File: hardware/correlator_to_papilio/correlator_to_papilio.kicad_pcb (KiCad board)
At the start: 4 copper layers, 67.6 x 53.3 mm, 2 parts, among them J1 Papilio Pro, U1 TART Correlator SODIMM

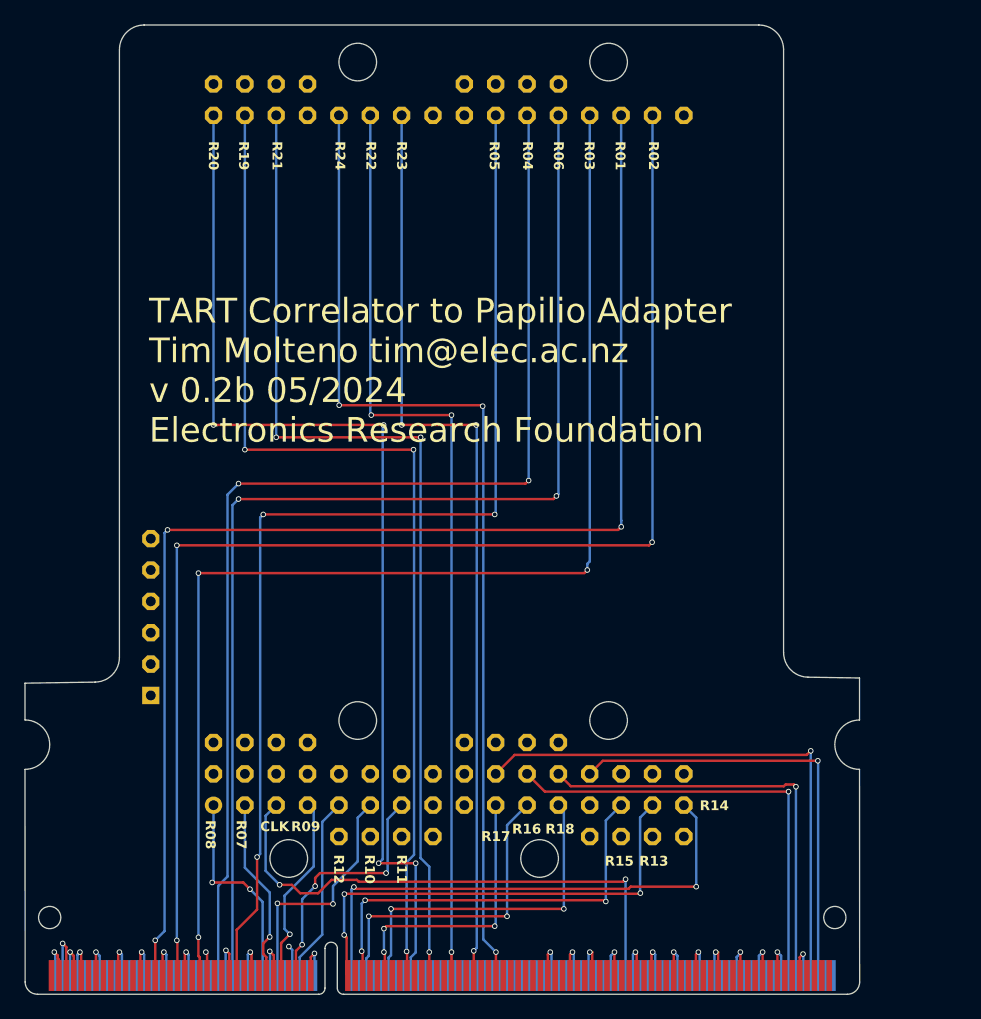
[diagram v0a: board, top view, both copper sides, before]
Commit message: Update the footprints and layout
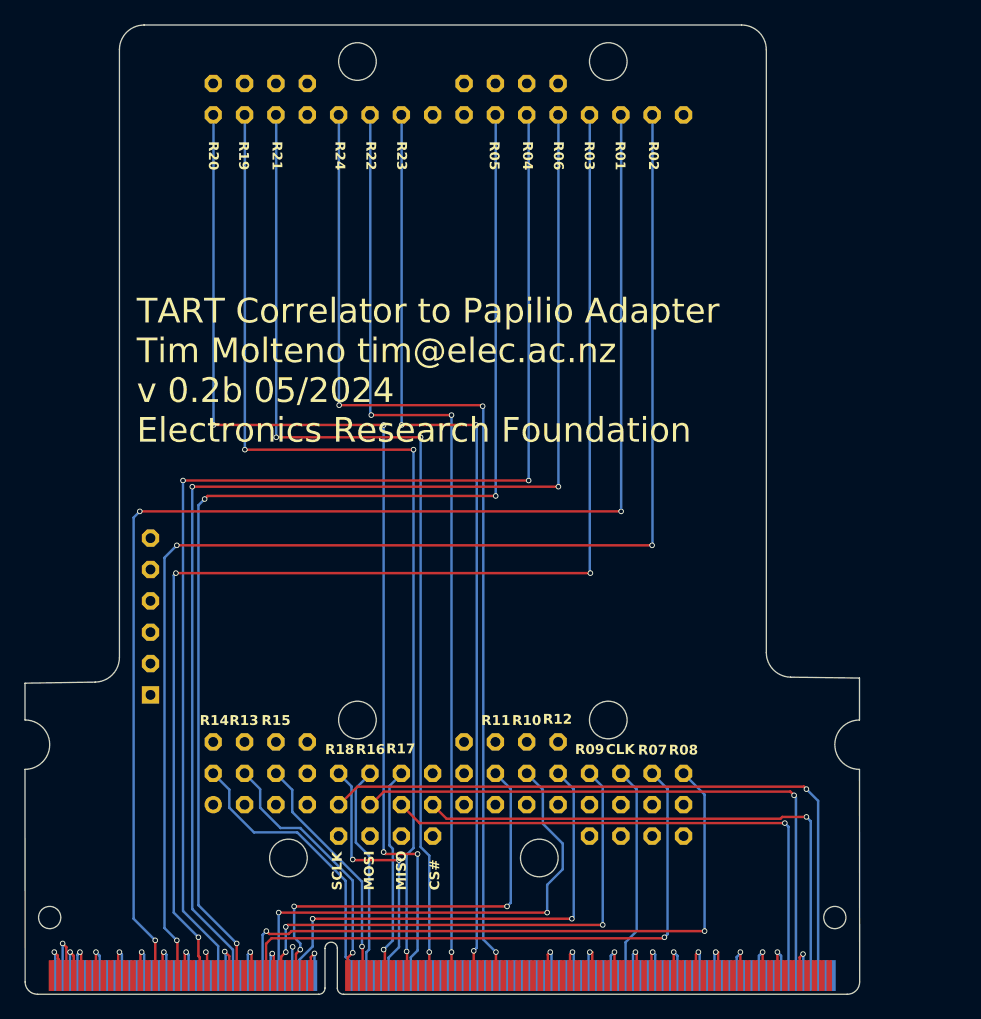
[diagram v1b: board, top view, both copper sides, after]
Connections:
- J1 pad A0: R14_I1 -> unconnected-(J1-PadA0)
- J1 pad A1: R13_I1 -> unconnected-(J1-PadA1)
- J1 pad A10: R10_I1 -> FPGA_MOSI
- J1 pad A11: R12_I1 -> FPGA_SCLK
- J1 pad A12: R09_I1 -> unconnected-(J1-PadA12)
- J1 pad A13: CLK_16 -> unconnected-(J1-PadA13)
- J1 pad A14: R07_I1 -> unconnected-(J1-PadA14)
- J1 pad A15: R08_I1 -> unconnected-(J1-PadA15)
- J1 pad A2: R15_I1 -> unconnected-(J1-PadA2)
- J1 pad A4: R18_I1 -> unconnected-(J1-PadA4)
- J1 pad A5: R16_I1 -> unconnected-(J1-PadA5)
- J1 pad A6: R17_I1 -> unconnected-(J1-PadA6)
- J1 pad A8: unconnected-(J1-PadA8) -> FPGA_CS#
- J1 pad A9: R11_I1 -> FPGA_MISO
- J1 pad B0: unconnected-(J1-PadB0) -> R14_I1
- J1 pad B1: unconnected-(J1-PadB1) -> R13_I1
- J1 pad B10: FPGA_MISO -> R10_I1
- J1 pad B11: FPGA_MOSI -> R12_I1
- J1 pad B12: FPGA_SCLK -> R09_I1
- J1 pad B13: unconnected-(J1-PadB13) -> CLK_16
- J1 pad B14: unconnected-(J1-PadB14) -> R07_I1
- J1 pad B15: unconnected-(J1-PadB15) -> R08_I1
- J1 pad B2: unconnected-(J1-PadB2) -> R15_I1
- J1 pad B4: unconnected-(J1-PadB4) -> R18_I1
- J1 pad B5: unconnected-(J1-PadB5) -> R16_I1
- J1 pad B6: unconnected-(J1-PadB6) -> R17_I1
- J1 pad B9: FPGA_CS# -> R11_I1
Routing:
- net R08_I1: track 17.0 -> 52.9 mm
- net R07_I1: track 15.0 -> 48.9 mm
- net R09_I1: track 15.5 -> 42.5 mm, vias 1 -> 3
- net CLK_16: track 44.0 -> 17.2 mm, vias 2 -> 0
- net R12_I1: track 15.1 -> 38.4 mm, vias 0 -> 2
- net R10_I1: track 19.6 -> 39.9 mm
- net R14_I1: track 42.1 -> 23.0 mm, vias 2 -> 0
- net FPGA_SCLK: track 36.3 -> 54.1 mm
- net R13_I1: track 38.3 -> 21.1 mm, vias 3 -> 1
- net R15_I1: track 34.1 -> 19.2 mm, vias 3 -> 1
- net FPGA_MOSI: track 35.1 -> 49.6 mm
- net R11_I1: track 20.5 -> 34.6 mm
- net R16_I1: track 25.8 -> 17.4 mm, vias 2 -> 0
- net FPGA_MISO: track 36.7 -> 44.1 mm
- net R18_I1: track 28.1 -> 20.9 mm
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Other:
- outline, holes or cut-outs redrawn
- board text added: "CS#"
- board text added: "MISO"
- board text added: "MOSI"
- board text added: "SCLK"

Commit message: Fix radio 4, and radio 7 being on the wrong pins
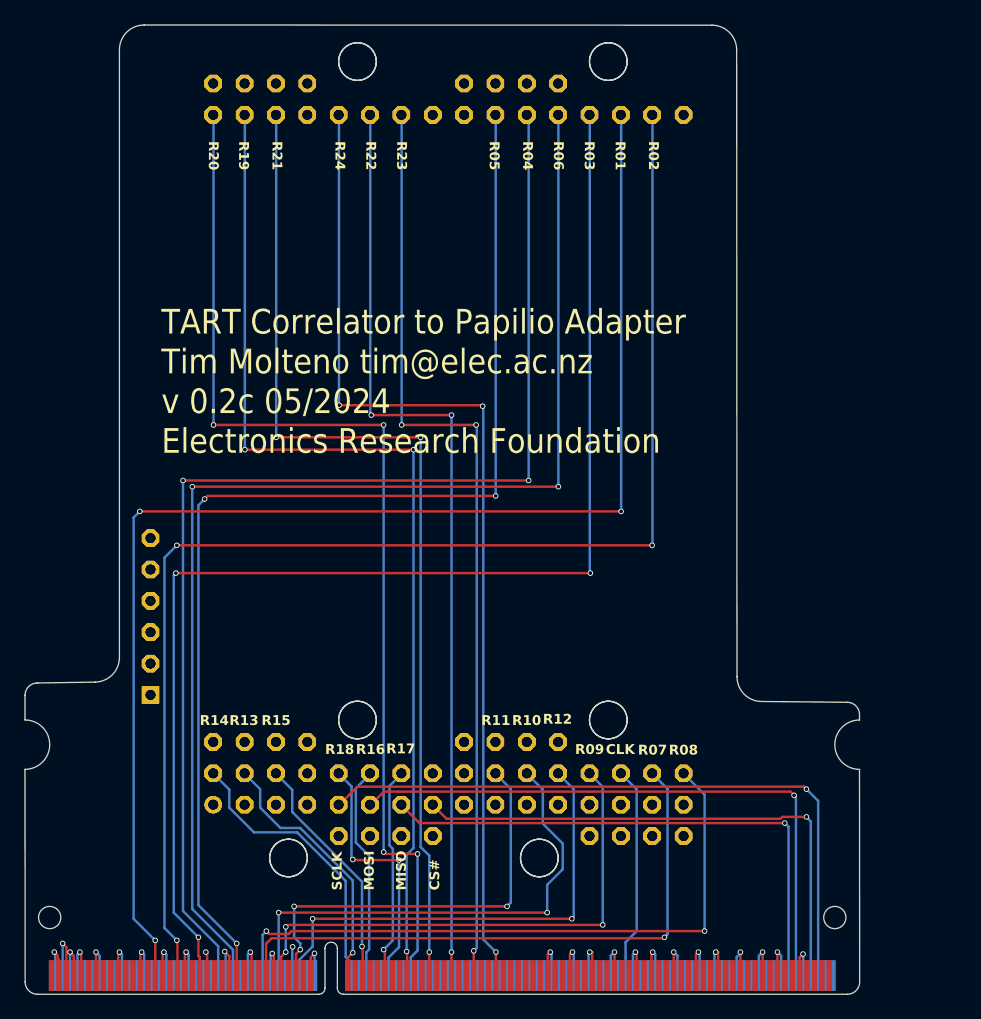
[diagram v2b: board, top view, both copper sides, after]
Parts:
- added J2: Papilio Pro, TART_Library:PAPILIO_PRO, B.Cu at (126.2, 111.8)
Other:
- board size 67.6 x 53.3 mm -> 67.6 x 56.3 mm
- board text added: "TART Correlator to Papilio Adapter Tim Molteno tim@elec.ac.nz v 0.2c 05/2024 Electronics Research Foundation"
- board text removed: "TART Correlator to Papilio Adapter Tim Molteno tim@elec.ac.nz v 0.2b 05/2024 Electronics Research Foundation"

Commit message: Updated to version c
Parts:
- removed J1: Papilio Pro, TART_Library:PAPILIO_PRO
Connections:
- U1 pad 46: R04_I1 -> unconnected-(U1-R04_Q1-Pad46)
- U1 pad 47: unconnected-(U1-R04_I1-Pad47) -> R04_I1
- U1 pad 57: unconnected-(U1-R07_Q1-Pad57) -> R07_I1
- U1 pad 59: R07_I1 -> unconnected-(U1-R07_Q1-Pad59)
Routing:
- net R04_I1: track 98.9 -> 99.1 mm, vias 2 -> 3
